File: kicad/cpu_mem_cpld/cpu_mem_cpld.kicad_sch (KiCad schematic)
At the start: 44 parts, among them CON1 BARREL_JACK, J1 USB, J3 DB9, SW1 SW_PUSH, U1 W65C02SxPL, U10 74HC245, U11 16550, U13 MAX232, U2 XC95108PC84, U3 28C256, U4 IS61C5128AS-25QLI, U5 74LS06, U6 LM555N, U9 74HC245, X1 OSC, X2 OSC

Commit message: remove all global labels
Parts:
- RN1: value R_Network04 -> 3k3
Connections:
- net ~{CS_UART2}: now reaches U2.56 (P56)
- net RDY renamed CPU_RDY
- net ~{CS_VDP} renamed ~{CSR_VDP}
- net ~{RW} renamed CPU_R~{W}
- net CPU_R~{W}: no longer U10.1 (A->B)
- new net CPU_RW: U10.1 (A->B)
- no-connect marks 22 -> 21
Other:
- sheet Connector ports: added RDY, ~{CS_OPL}, ~{CS_UART2}, ~{CS_VDP}, ~{CS_VIA}, ~{IRQ}, ~{NMI}, ~{RESET}; removed none
- moved on the sheet: R2

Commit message: cpu cpld 512
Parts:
- added unit 6 of U5
- added unit 7 of U5
- added unit 4 of U5
- added unit 5 of U5
- C1: value 100n -> (none); footprint Capacitor_THT:C_Disc_D3.0mm_W2.0mm_P2.50mm -> (none)
- U11: footprint Package_LCC:PLCC-44 -> Package_LCC:PLCC-44_THT-Socket
- U4: footprint Package_SO:SSOP-32_11.305x20.495mm_P1.27mm -> Package_DIP:DIP-32_W15.24mm_LongPads; symbol Memory_RAM:IS61C5128AS-25QLI -> Memory_RAM:AS6C4008-55PCN
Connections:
- net EXT_A13 is gone; now on net CPU_A13: U2.84 (P84), U3.26 (A13), U4.28 (A13)
- net CPU_A0: now also U2.81 (P81); no longer U2.24 (P24)
- net CPU_A1: now also U2.15 (P15); no longer U2.25 (P25)
- net CPU_A10: now also U2.65 (P65); no longer U2.39 (P39)
- net CPU_A11: now also U2.66 (P66); no longer U2.40 (P40)
- net CPU_A12: now also U2.56 (P56); no longer U2.41 (P41)
- net CPU_A13: no longer U2.43 (P43)
- net CPU_A14: now also U2.13 (P13); no longer U2.44 (P44)
- net CPU_A15: now also U2.3 (P3); no longer U2.45 (P45)
- net CPU_A2: no longer U2.26 (P26)
- net CPU_A3: no longer U2.31 (P31)
- net CPU_A4: now also U2.48 (P48); no longer U2.32 (P32)
- net CPU_A5: now also U2.70 (P70); no longer U2.33 (P33)
- net CPU_A6: now also U2.53 (P53); no longer U2.34 (P34)
- net CPU_A7: now also U2.83 (P83); no longer U2.35 (P35)
- net CPU_A8: now also U2.17 (P17); no longer U2.36 (P36)
- net CPU_A9: now also U2.44 (P44); no longer U2.37 (P37)
- net CPU_RDY: now also U2.14 (P14); no longer U2.46 (P46)
- net CPU_R~{W}: now also U2.71 (P71); no longer U2.50 (P50)
- net D2: now also U2.46 (P46); no longer U2.3 (P3)
- net D3: now also U2.72 (P72); no longer U2.4 (P4)
- net D4: now also U2.68 (P68); no longer U2.5 (P5)
- net D5: now also U2.82 (P82); no longer U2.6 (P6)
- net D6: now also U2.23 (P23); no longer U2.7 (P7)
- net D7: now also U2.79 (P79); no longer U2.10 (I/O/GCK2)
- net EXT_A14: now also U2.5 (P5); no longer U2.83 (P83)
- net EXT_A15: now also U2.18 (P18); no longer U2.82 (P82)
- net EXT_A16: now also U2.47 (P47); no longer U2.81 (P81)
- net EXT_A17: now also U2.52 (P52), U4.30 (A17); no longer U2.80 (P80), U4.1 (A17)
- net EXT_A18: now also U2.61 (P61), U4.1 (A18); no longer U2.79 (P79), U4.30 (A18)
- net GND: now also U5.11, U5.13, U5.7 (GND), U5.9; no longer U2.11 (P11), U2.12 (I/O/GCK3), U2.13 (P13), U2.14 (P14), U2.15 (P15), U2.17 (P17), U2.18 (P18), U2.19 (P19), U2.20 (P20), U2.21 (P21), U2.23 (P23), U2.61 (P61), U2.62 (P62), U2.63 (P63), U2.65 (P65), U2.66 (P66), U2.67 (P67), U2.68 (P68), U2.69 (P69), U2.70 (P70), U2.71 (P71), U2.72 (P72), U2.75 (P75), U2.76 (I/O/GTS1), U2.77 (I/O/GTS2)
- net PHI2: now also U2.19 (P19); no longer U2.51 (P51)
- net VCC: now also U5.14 (VCC)
- net ~{CSR_VDP}: no longer U2.55 (P55)
- net ~{CS_OPL}: now also U2.35 (P35); no longer U2.58 (P58)
- net ~{CS_RAM}: now also U2.25 (P25); no longer U2.52 (P52)
- net ~{CS_ROM}: now also U2.31 (P31); no longer U2.53 (P53)
- net ~{CS_UART2}: no longer U2.56 (P56)
- net ~{CS_UART}: now also U2.26 (P26); no longer U2.54 (P54)
- net ~{CS_VIA}: now also U2.43 (P43); no longer U2.57 (P57)
- net ~{OE}: now also U2.37 (P37); no longer U2.48 (P48)
- net ~{WE}: now also U2.39 (P39); no longer U2.47 (P47)
- new net ~{CS_VDP}: U2.33 (P33)
- no-connect marks 21 -> 54
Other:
- moved on the sheet: JTAG1, RN1, U2

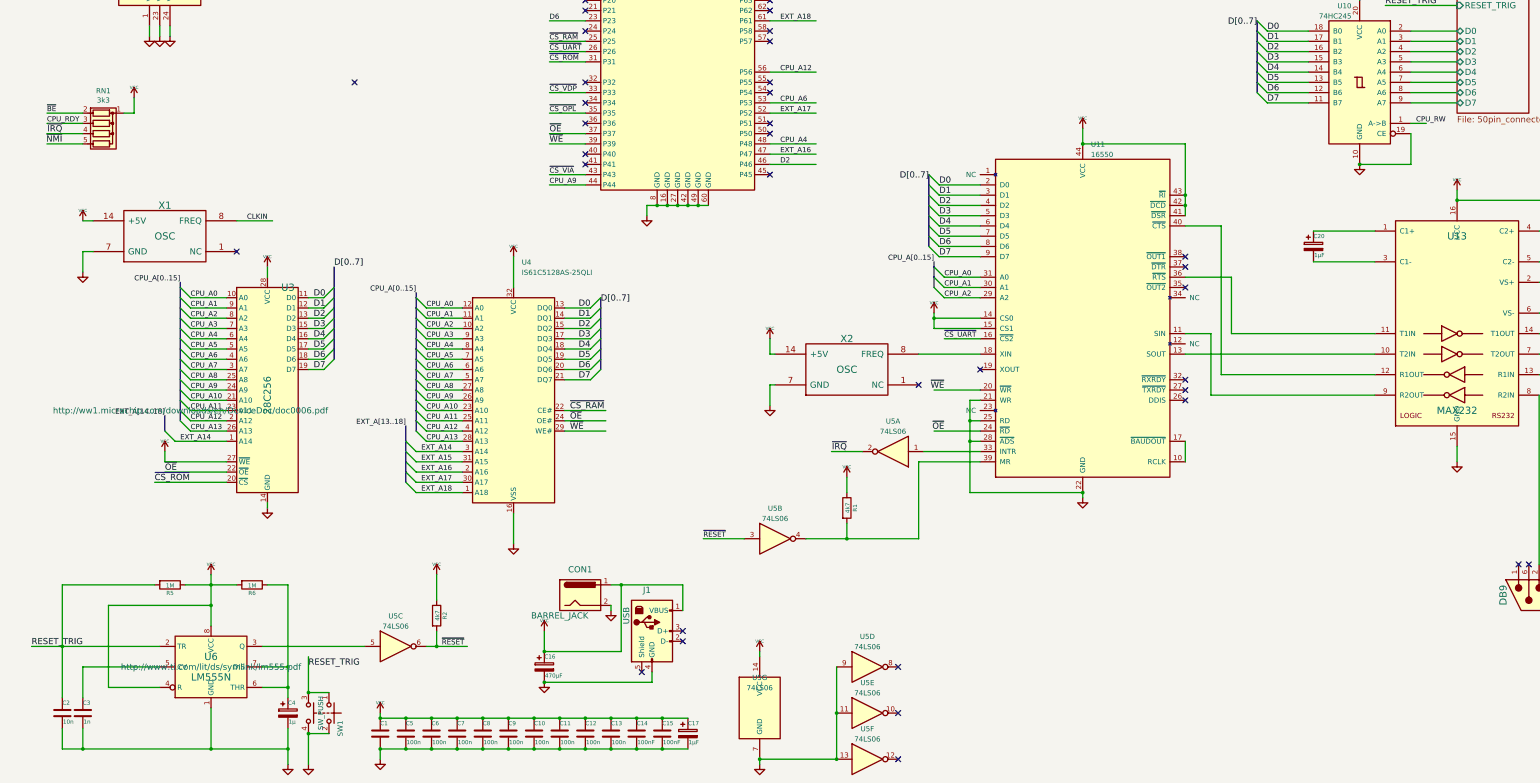
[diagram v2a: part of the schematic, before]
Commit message: added cs_uart2, /WE for EEPROM
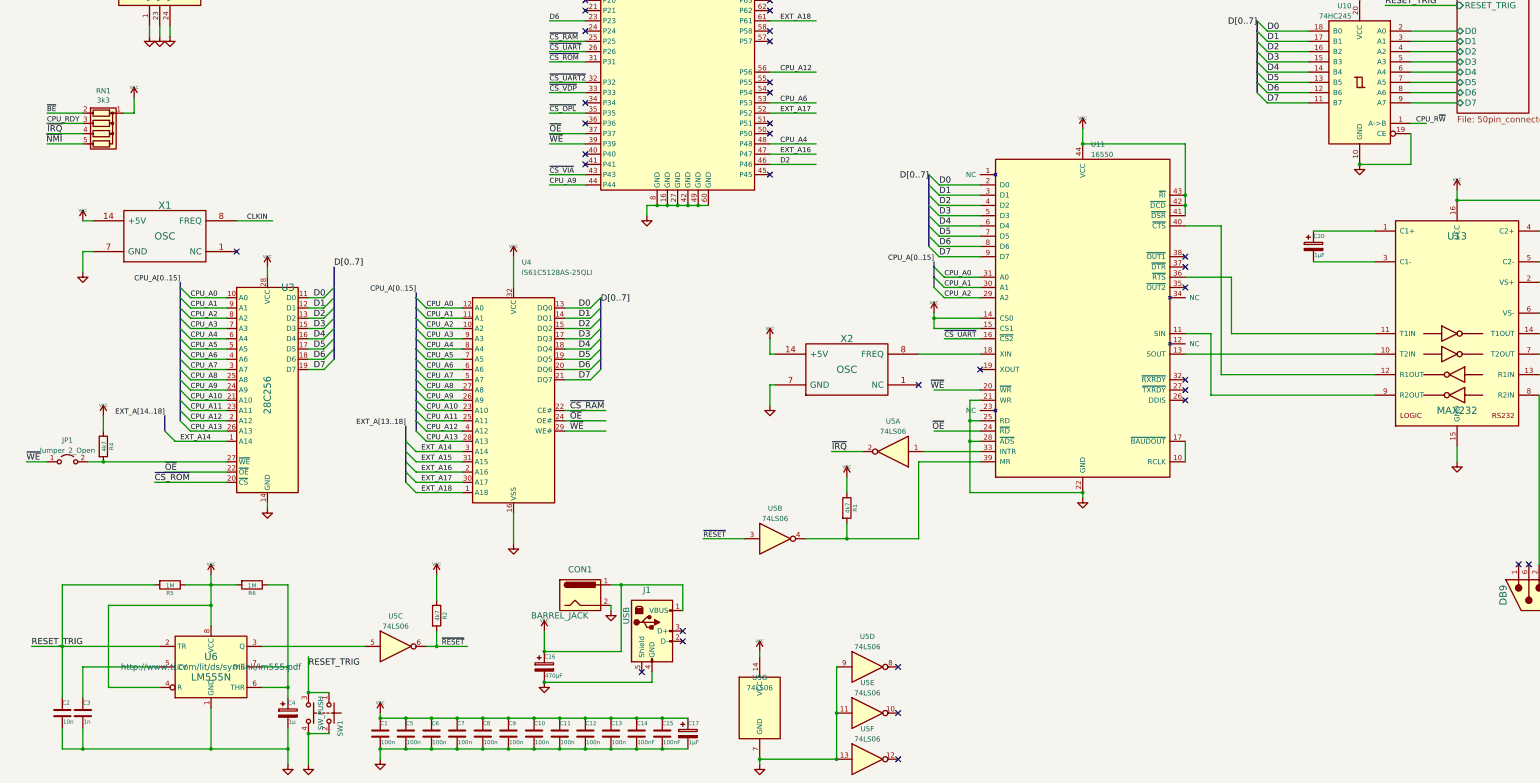
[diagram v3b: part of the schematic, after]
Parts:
- added JP1: Jumper_2_Open, Connector_PinHeader_2.54mm:PinHeader_2x01_P2.54mm_Vertical, symbol Jumper:Jumper_2_Open
- added R4: 4k7, Resistor_THT:R_Axial_DIN0204_L3.6mm_D1.6mm_P5.08mm_Horizontal, symbol Device:R
- C1: value (none) -> 100n; footprint (none) -> Capacitor_SMD:C_1206_3216Metric_Pad1.33x1.80mm_HandSolder
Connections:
- net CPU_RW is gone; now on net CPU_R~{W}: U10.1 (A->B)
- net VCC: now also R4.1; no longer U3.27 (~{WE})
- net ~{CS_UART2}: now also U2.32 (P32)
- net ~{WE}: now also JP1.1 (A)
- new net: JP1.2 (B), R4.2, U3.27 (~{WE})
- no-connect marks 54 -> 52
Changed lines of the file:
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@@
   (junction (at 58.42 275.59) (diameter 0) (color 0 0 0 0)
   )
+  (junction (at 31.75 204.47) (diameter 0) (color 0 0 0 0)
+  )
   (junction (at 100.33 267.97) (diameter 0) (color 0 0 0 0)
   )
@@
   (no_connect (at 196.85 92.71))
   (no_connect (at 196.85 100.33))
-  (no_connect (at 151.13 110.49))
   (no_connect (at 151.13 115.57))
   (no_connect (at 151.13 128.27))
@@
   (no_connect (at 175.26 246.38))
   (no_connect (at 30.48 87.63))
-  (no_connect (at 93.98 110.49))
   (no_connect (at 196.85 133.35))
   (no_connect (at 248.92 181.61))
@@
     (stroke (width 0) (type default) (color 0 0 0 0))
   )
+  (wire (pts (xy 31.75 204.47) (xy 62.23 204.47))
+    (stroke (width 0) (type default) (color 0 0 0 0))
+  )
   (wire (pts (xy 321.31 57.15) (xy 330.2 57.15))
     (stroke (width 0) (type default) (color 0 0 0 0))
@@
     (stroke (width 0) (type default) (color 0 0 0 0))
   )
+  (wire (pts (xy 142.24 110.49) (xy 151.13 110.49))
+    (stroke (width 0) (type default) (color 0 0 0 0))
+  )
   (wire (pts (xy 196.85 190.5) (xy 196.85 185.42))
     (stroke (width 0) (type default) (color 0 0 0 0))
@@
     (stroke (width 0) (type default) (color 0 0 0 0))
   )
-  (wire (pts (xy 46.99 201.93) (xy 46.99 204.47))
-    (stroke (width 0) (type default) (color 0 0 0 0))
-  )
   (bus (pts (xy 50.8 166.37) (xy 50.8 168.91))
     (stroke (width 0) (type default) (color 0 0 0 0))
@@
     (stroke (width 0) (type default) (color 0 0 0 0))
   )
+  (wire (pts (xy 31.75 193.04) (xy 31.75 196.85))
+    (stroke (width 0) (type default) (color 0 0 0 0))
+  )
   (wire (pts (xy 246.38 212.09) (xy 274.32 212.09))
     (stroke (width 0) (type default) (color 0 0 0 0))
@@
     (stroke (width 0) (type default) (color 0 0 0 0))
   )
+  (wire (pts (xy 12.7 204.47) (xy 17.78 204.47))
+    (stroke (width 0) (type default) (color 0 0 0 0))
+  )
   (wire (pts (xy 311.15 172.72) (xy 311.15 158.75))
     (stroke (width 0) (type default) (color 0 0 0 0))
@@
     (stroke (width 0) (type default) (color 0 0 0 0))
   )
-  (wire (pts (xy 46.99 204.47) (xy 62.23 204.47))
+  (wire (pts (xy 27.94 204.47) (xy 31.75 204.47))
     (stroke (width 0) (type default) (color 0 0 0 0))
   )
@@
     (effects (font (size 1.524 1.524)) (justify right bottom))
   )
+  (label "~{WE}" (at 12.7 204.47 0)
+    (effects (font (size 1.524 1.524)) (justify left bottom))
+  )
   (label "CPU_A15" (at 236.22 64.77 0)
     (effects (font (size 1.27 1.27)) (justify left bottom))
@@
     (effects (font (size 1.27 1.27)) (justify left bottom))
   )
+  (label "~{CS_UART2}" (at 142.24 110.49 0)
+    (effects (font (size 1.27 1.27)) (justify left bottom))
+  )
   (label "CPU_A10" (at 53.34 189.23 0)
     (effects (font (size 1.27 1.27)) (justify left bottom))
@@
     (effects (font (size 1.524 1.524)) (justify right bottom))
   )
+  (label "CPU_R~{W}" (at 356.87 120.65 0)
+    (effects (font (size 1.27 1.27)) (justify left bottom))
+  )
   (label "~{OE}" (at 323.85 49.53 180)
     (effects (font (size 1.524 1.524)) (justify right bottom))
@@
     (effects (font (size 1.524 1.524)) (justify left bottom))
   )
-  (label "CPU_RW" (at 356.87 120.65 0)
-    (effects (font (size 1.27 1.27)) (justify left bottom))
-  )
   (label "D1" (at 320.04 100.33 0)
     (effects (font (size 1.524 1.524)) (justify left bottom))
@@
       (effects (font (size 1.016 1.016)) (justify left))
     )
-    (property "Value" "" (id 1) (at 100.4824 273.939 0)
+    (property "Value" "100n" (id 1) (at 100.4824 273.939 0)
       (effects (font (size 1.016 1.016)) (justify left))
     )
-    (property "Footprint" "" (id 2) (at 101.2952 275.59 0)
+    (property "Footprint" "Capacitor_SMD:C_1206_3216Metric_Pad1.33x1.80mm_HandSolder" (id 2) (at 101.2952 275.59 0)
       (effects (font (size 0.762 0.762)) hide)
     )
@@
     )
     (property "Datasheet" "http://ww1.microchip.com/downloads/en/DeviceDoc/doc0006.pdf" (id 3) (at 53.34 191.77 0)
-      (effects (font (size 1.524 1.524)))
+      (effects (font (size 1.524 1.524)) hide)
     )
     (pin "1")
@@
     (pin "2")
   )
-  (symbol (lib_id "power:VCC") (at 46.99 201.93 0) (unit 1)
+  (symbol (lib_id "power:VCC") (at 31.75 193.04 0) (unit 1)
     (in_bom yes) (on_board yes)
-    (property "Reference" "#PWR013" (id 0) (at 46.99 199.39 0)
+    (property "Reference" "#PWR013" (id 0) (at 31.75 190.5 0)
       (effects (font (size 0.762 0.762)) hide)
     )
-    (property "Value" "VCC" (id 1) (at 46.99 199.39 0)
+    (property "Value" "VCC" (id 1) (at 31.75 190.5 0)
       (effects (font (size 0.762 0.762)))
     )
-    (property "Footprint" "" (id 2) (at 46.99 201.93 0)
+    (property "Footprint" "" (id 2) (at 31.75 193.04 0)
       (effects (font (size 1.524 1.524)))
     )
-    (property "Datasheet" "" (id 3) (at 46.99 201.93 0)
+    (property "Datasheet" "" (id 3) (at 31.75 193.04 0)
       (effects (font (size 1.524 1.524)))
     )
@@
     (pin "2")
   )
+  (symbol (lib_id "Device:R") (at 31.75 200.66 0) (unit 1)
+    (in_bom yes) (on_board yes)
+    (property "Reference" "R4" (id 0) (at 33.782 200.66 90)
+      (effects (font (size 1.016 1.016)))
+    )
+    (property "Value" "4k7" (id 1) (at 31.9278 200.6346 90)
+      (effects (font (size 1.016 1.016)))
+    )
+    (property "Footprint" "Resistor_THT:R_Axial_DIN0204_L3.6mm_D1.6mm_P5.08mm_Horizontal" (id 2) (at 29.972 200.66 90)
+      (effects (font (size 1.27 1.27)) hide)
+    )
+    (property "Datasheet" "~" (id 3) (at 31.75 200.66 0)
+      (effects (font (size 1.27 1.27)) hide)
+    )
+    (pin "1")
+    (pin "2")
+  )
   (symbol (lib_id "Device:R") (at 215.9 215.9 0) (unit 1)
     (in_bom yes) (on_board yes)
@@
     (pin "1")
   )
+  (symbol (lib_id "Jumper:Jumper_2_Open") (at 22.86 204.47 0) (unit 1)
+    (in_bom yes) (on_board yes) (fields_autoplaced)
+    (property "Reference" "JP1" (id 0) (at 22.86 199.1192 0))
+    (property "Value" "Jumper_2_Open" (id 1) (at 22.86 201.6561 0))
+    (property "Footprint" "Connector_PinHeader_2.54mm:PinHeader_2x01_P2.54mm_Vertical" (id 2) (at 22.86 204.47 0)
+      (effects (font (size 1.27 1.27)) hide)
+    )
+    (property "Datasheet" "~" (id 3) (at 22.86 204.47 0)
+      (effects (font (size 1.27 1.27)) hide)
+    )
+    (pin "1")
+    (pin "2")
+  )
   (symbol (lib_id "power:VCC") (at 367.03 137.16 0) (unit 1)
     (in_bom yes) (on_board yes)
@@
       (reference "J3") (unit 1) (value "DB9") (footprint "Connector_Dsub:DSUB-9_Male_Horizontal_P2.77x2.84mm_EdgePinOffset4.94mm_Housed_MountingHolesOffset7.48mm")
     )
+    (path "/b11517e7-c73e-41e7-81e8-b92d482d3709"
+      (reference "JP1") (unit 1) (value "Jumper_2_Open") (footprint "Connector_PinHeader_2.54mm:PinHeader_2x01_P2.54mm_Vertical")
+    )
     (path "/00000000-0000-0000-0000-000062aa2d6c"
       (reference "JTAG1") (unit 1) (value "Conn_01x06_Male") (footprint "Connector_PinHeader_2.54mm:PinHeader_1x06_P2.54mm_Vertical")
@@
       (reference "R3") (unit 1) (value "3k3") (footprint "Resistor_THT:R_Axial_DIN0204_L3.6mm_D1.6mm_P5.08mm_Horizontal")
     )
+    (path "/02cd4006-0b38-45e5-a021-fce1decf54d3"
+      (reference "R4") (unit 1) (value "4k7") (footprint "Resistor_THT:R_Axial_DIN0204_L3.6mm_D1.6mm_P5.08mm_Horizontal")
+    )
     (path "/00000000-0000-0000-0000-000054136b39"

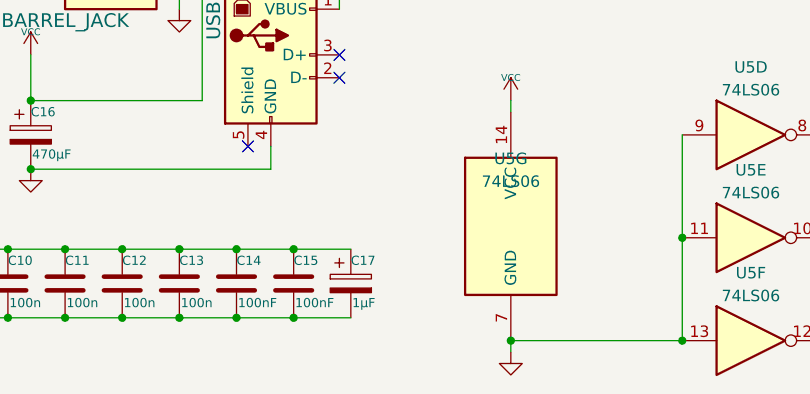
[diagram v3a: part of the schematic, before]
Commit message: extra capacitor, revision text
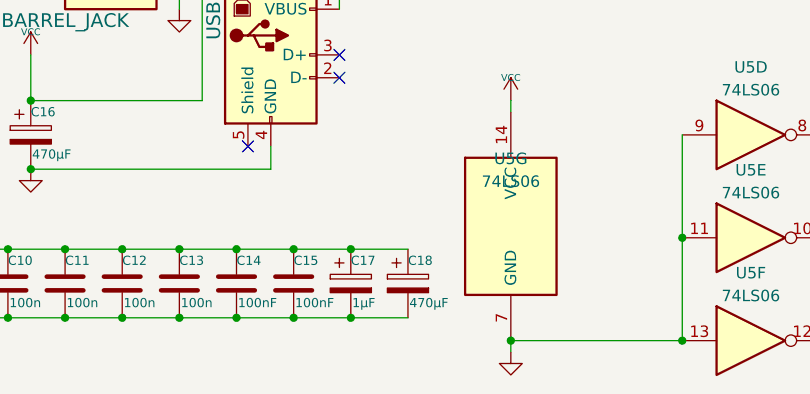
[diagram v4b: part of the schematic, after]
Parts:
- added C18: 470µF, Capacitor_THT:CP_Radial_D10.0mm_P5.00mm, symbol Device:C_Polarized
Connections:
- net GND: now also C18.2
- net VCC: now also C18.1
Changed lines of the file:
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@@
   (junction (at 237.49 168.91) (diameter 0) (color 0 0 0 0)
   )
+  (junction (at 176.53 267.97) (diameter 0) (color 0 0 0 0)
+  )
   (junction (at 151.13 275.59) (diameter 0) (color 0 0 0 0)
   )
@@
   (junction (at 132.08 275.59) (diameter 0) (color 0 0 0 0)
   )
+  (junction (at 176.53 275.59) (diameter 0) (color 0 0 0 0)
+  )
   (junction (at 106.68 267.97) (diameter 0) (color 0 0 0 0)
   )
@@
     (stroke (width 0) (type default) (color 0 0 0 0))
   )
+  (wire (pts (xy 176.53 267.97) (xy 182.88 267.97))
+    (stroke (width 0) (type default) (color 0 0 0 0))
+  )
   (wire (pts (xy 120.65 173.99) (xy 111.76 173.99))
     (stroke (width 0) (type default) (color 0 0 0 0))
@@
     (stroke (width 0) (type default) (color 0 0 0 0))
   )
+  (wire (pts (xy 176.53 275.59) (xy 182.88 275.59))
+    (stroke (width 0) (type default) (color 0 0 0 0))
+  )
   (wire (pts (xy 82.55 271.78) (xy 82.55 279.4))
     (stroke (width 0) (type default) (color 0 0 0 0))
@@
     (pin "7")
   )
+  (symbol (lib_id "Device:C_Polarized") (at 182.88 271.78 0) (unit 1)
+    (in_bom yes) (on_board yes)
+    (property "Reference" "C18" (id 0) (at 182.88 269.24 0)
+      (effects (font (size 1.016 1.016)) (justify left))
+    )
+    (property "Value" "470µF" (id 1) (at 183.0324 273.939 0)
+      (effects (font (size 1.016 1.016)) (justify left))
+    )
+    (property "Footprint" "Capacitor_THT:CP_Radial_D10.0mm_P5.00mm" (id 2) (at 183.8452 275.59 0)
+      (effects (font (size 1.27 1.27)) hide)
+    )
+    (property "Datasheet" "~" (id 3) (at 182.88 271.78 0)
+      (effects (font (size 1.27 1.27)) hide)
+    )
+    (pin "1")
+    (pin "2")
+  )
   (symbol (lib_id "Memory_RAM:AS6C4008-55PCN") (at 133.35 189.23 0) (unit 1)
     (in_bom yes) (on_board yes) (fields_autoplaced)
@@
       (reference "C17") (unit 1) (value "1µF") (footprint "Capacitor_THT:CP_Radial_D4.0mm_P2.00mm")
     )
+    (path "/3f174f1b-c5af-4567-bc7b-fe1b01153944"
+      (reference "C18") (unit 1) (value "470µF") (footprint "Capacitor_THT:CP_Radial_D10.0mm_P5.00mm")
+    )
     (path "/952fddd1-6fb1-4be0-b5ed-09371300a61d"
